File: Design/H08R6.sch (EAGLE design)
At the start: 41 parts, among them P1 HEXABIT_17.32, U1 STM32G0B1CEU6N, U2 VL53L8CXV0GC_1, U3 LDK130PU18R, U4 TCK107AG,LF, U5 PI4ULS3V204ZBEX, U6 PI4ULS3V204ZBEX, X1 XTALL_CSTCE8M00G52

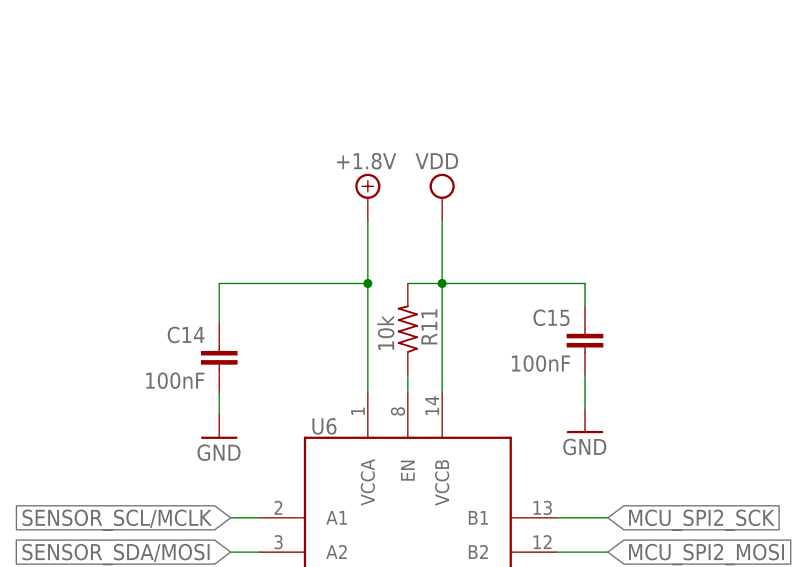
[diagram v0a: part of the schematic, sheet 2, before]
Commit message: Correct the EN pin of the level shifter IC referencing.
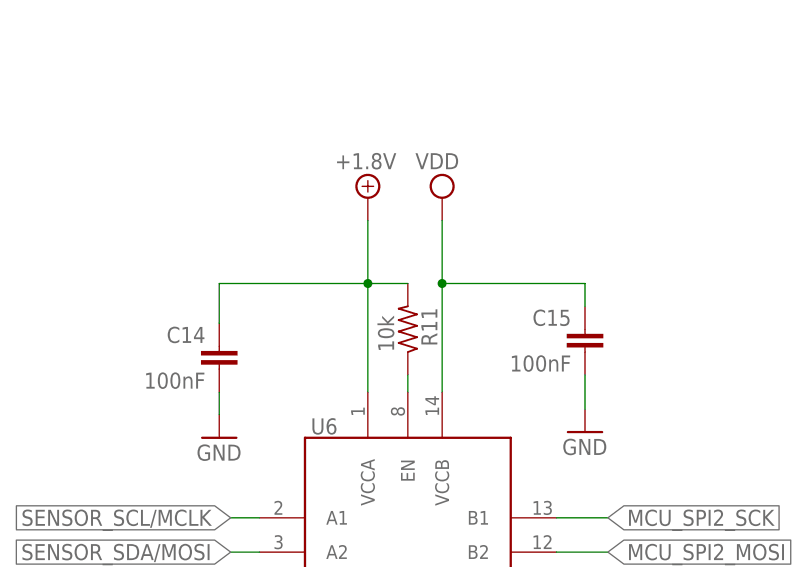
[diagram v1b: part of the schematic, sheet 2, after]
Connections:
- net +1.8V: now also R11.2
- net VDD: no longer R11.2
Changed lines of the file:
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@@
 <setting verticaltext="up"/>
 </settings>
-<grid distance="25" unitdist="mil" unit="mil" style="lines" multiple="1" display="no" altdistance="0.01" altunitdist="inch" altunit="inch"/>
+<grid distance="0.025" unitdist="inch" unit="inch" style="lines" multiple="1" display="no" altdistance="0.01" altunitdist="inch" altunit="inch"/>
 <layers>
 <layer number="1" name="Top" color="4" fill="1" visible="no" active="no"/>
@@
 <wire x1="173.355" y1="91.44" x2="173.355" y2="93.98" width="0.1524" layer="91"/>
 <wire x1="173.355" y1="93.98" x2="157.48" y2="93.98" width="0.1524" layer="91"/>
-<pinref part="R11" gate="G$1" pin="2"/>
-<wire x1="153.67" y1="93.98" x2="157.48" y2="93.98" width="0.1524" layer="91"/>
 <junction x="157.48" y="93.98"/>
 <pinref part="SUPPLY21" gate="G$1" pin="VDD"/>
@@
 <wire x1="149.225" y1="81.915" x2="149.225" y2="93.98" width="0.1524" layer="91"/>
 <junction x="149.225" y="93.98"/>
+<pinref part="R11" gate="G$1" pin="2"/>
+<wire x1="153.67" y1="93.98" x2="149.225" y2="93.98" width="0.1524" layer="91"/>
 </segment>
 </net>

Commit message: Update the description
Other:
- note added: "VL53L8 IR ToF LiDar Sensor"
- note removed: "IR ToF LiDar Sensor"
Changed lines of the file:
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@@
 <setting verticaltext="up"/>
 </settings>
-<grid distance="0.025" unitdist="inch" unit="inch" style="lines" multiple="1" display="no" altdistance="0.01" altunitdist="inch" altunit="inch"/>
+<grid distance="0.1" unitdist="inch" unit="inch" style="lines" multiple="1" display="no" altdistance="0.01" altunitdist="inch" altunit="inch"/>
 <layers>
 <layer number="1" name="Top" color="4" fill="1" visible="no" active="no"/>
@@
 <text x="199.4662" y="19.6342" size="1.9304" layer="100" font="vector">Title</text>
 <text x="180.9242" y="19.6342" size="1.9304" layer="102" font="vector">H08R6</text>
-<text x="179.2478" y="11.2014" size="1.9304" layer="101" font="vector"> IR ToF LiDar Sensor</text>
+<text x="174.1678" y="11.2014" size="1.9304" layer="101" font="vector">VL53L8 IR ToF LiDar Sensor</text>
 <text x="206.3242" y="19.6342" size="1.9304" layer="101" font="vector">H08R6_Backend</text>
 <wire x1="168.91" y1="3.81" x2="168.91" y2="8.128" width="0.1524" layer="205"/>
@@
 <text x="199.4662" y="19.6342" size="1.9304" layer="100" font="vector">Title</text>
 <text x="180.9242" y="19.6342" size="1.9304" layer="102" font="vector">H08R6</text>
-<text x="179.2478" y="11.2014" size="1.9304" layer="101" font="vector"> IR ToF LiDar Sensor</text>
+<text x="174.1678" y="11.2014" size="1.9304" layer="101" font="vector"> VL53L8 IR ToF LiDar Sensor</text>
 <text x="206.3242" y="19.6342" size="1.9304" layer="101" font="vector">H08R6_Frontend</text>
 <wire x1="168.91" y1="3.81" x2="168.91" y2="8.128" width="0.1524" layer="205"/>

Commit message: -Fix missing connection -Add TVS -Update the logo -Fix clearence and soldermask
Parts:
- added D2: BOURNS_CDSOD323-T03SCBOURNS_CDSOD323-T03SC_0_0, HEXABITZ_RCLS:BOURNS_CDSOD323-T03SCBOURNS_CDSOD323-T03SC_0_0
- added TRIMBLE-LOGO1: HEXA-LOGO, HEXABITZ_USER_INTERFACE_PARTS:HEXA-LOGO
- C11: device HEXABITZ_RCLS:C-0402 -> HEXABITZ_RCLS:C-0603
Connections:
- net GND: now also D2.C
- net VDD: now also D2.A

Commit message: -Change the MCU footprint to STM32G0B1CEU6
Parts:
- removed C3: 100nF, HEXABITZ_RCLS:C-0402
- removed C4: 4.7uF, HEXABITZ_RCLS:C-0603-POL
- U1: value STM32G0B1CEU6N -> STM32G0B1CEU6QFN_B1CEU6_STM-L; device HEXABITZ_ICs:STM32G0B1CEU6N -> HEXABITZ_ICs:STM32G0B1CEU6QFN_B1CEU6_STM-L
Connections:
- net GND: no longer C3.2, C4.2, U1.EPAD
- net VDD: no longer C3.1, C4.1, U1.VDDIO2
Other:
- moved on the sheet: D2
